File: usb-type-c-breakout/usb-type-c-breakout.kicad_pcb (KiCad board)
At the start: 4 copper layers, 29.5 x 47.5 mm, 44 parts, among them J10 USB_B_Micro, J11 USB_C_Plug, J12 Conn_02x04_Odd_Even, J2 Conn_Coaxial, J3 Conn_Coaxial, J4 Conn_Coaxial, J5 Conn_Coaxial, J6 Conn_Coaxial, J7 Conn_Coaxial, J8 Conn_Coaxial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

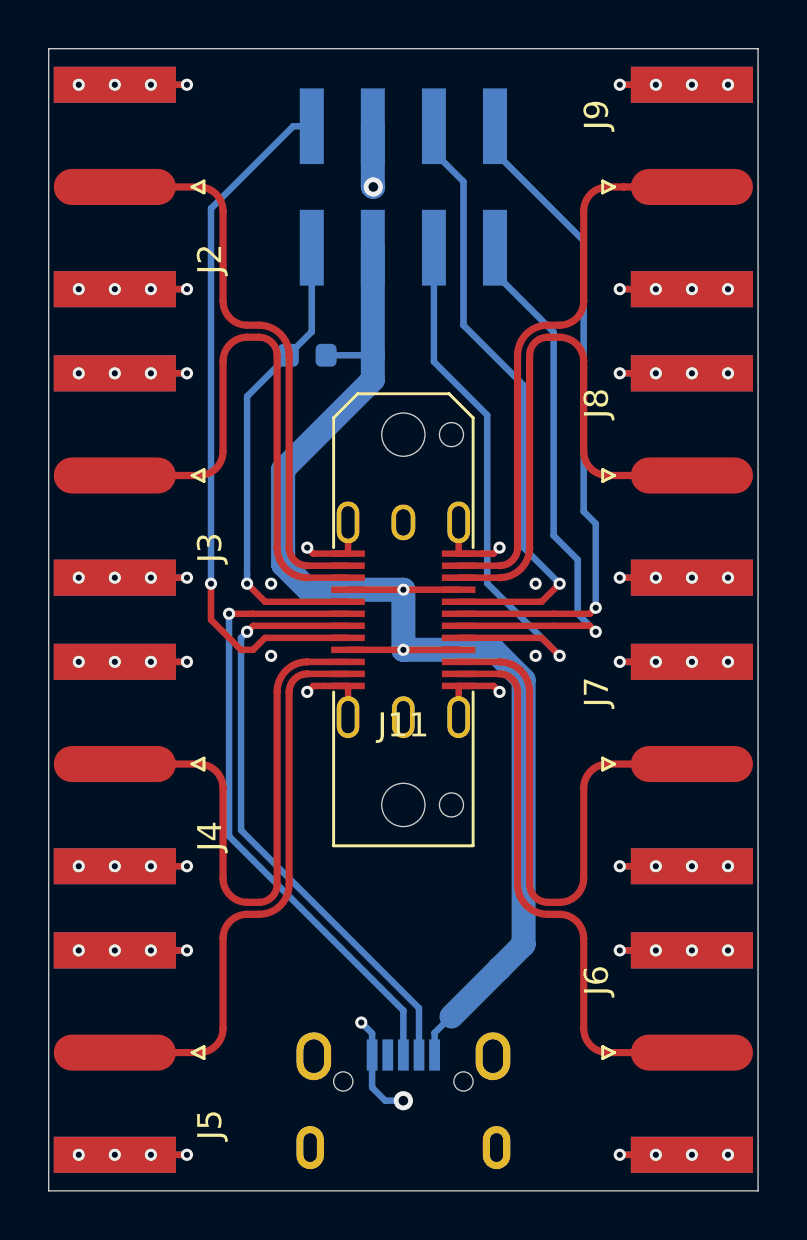
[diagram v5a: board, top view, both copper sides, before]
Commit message: assigned curve pads, added silk notes
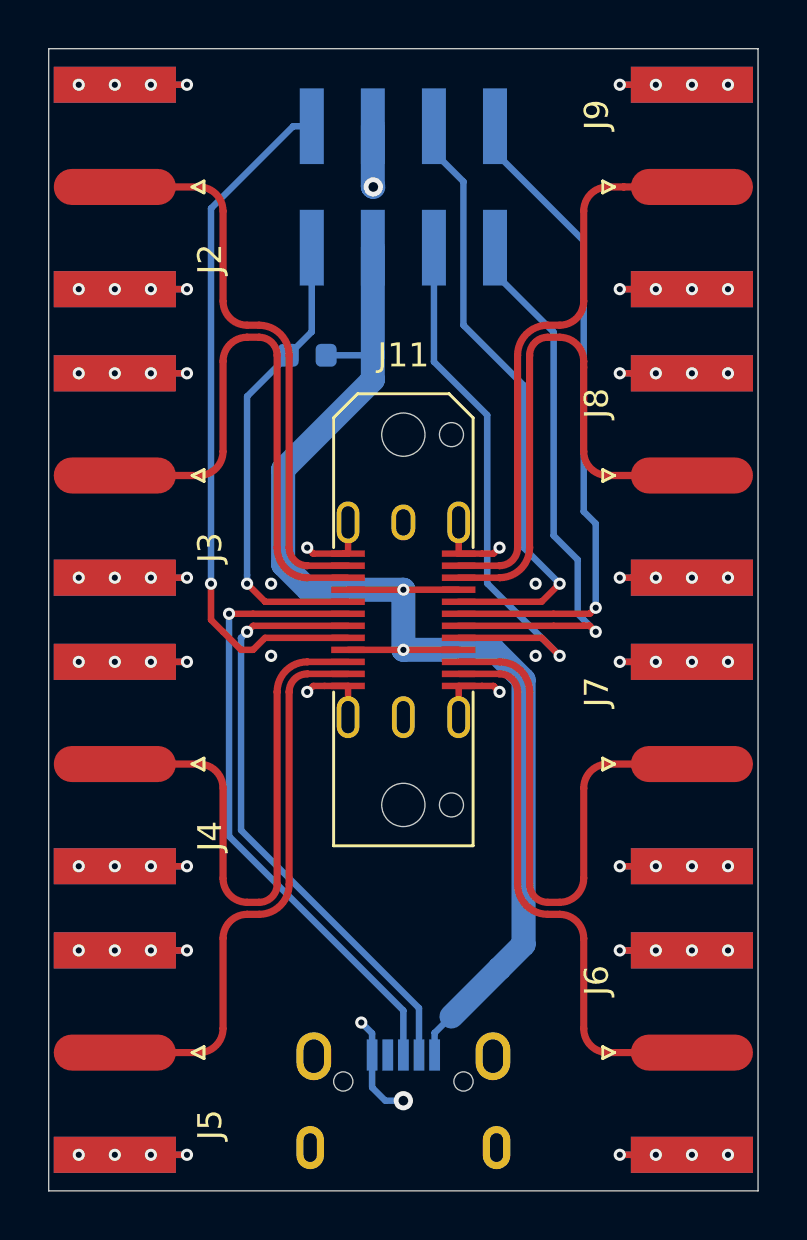
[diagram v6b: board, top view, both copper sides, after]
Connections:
- REF** pad 1: (no net) -> Net-(J11-PadB11) (x4)
- REF** pad 1: (no net) -> Net-(J11-PadA11) (x4)
- REF** pad 1: (no net) -> Net-(J11-PadA10) (x4)
- REF** pad 1: (no net) -> Net-(J11-PadA3) (x4)
- REF** pad 1: (no net) -> Net-(J11-PadA2) (x4)
- REF** pad 1: (no net) -> Net-(J11-PadB2) (x4)
- REF** pad 1: (no net) -> Net-(J11-PadB3) (x4)
- REF** pad 1: (no net) -> Net-(J11-PadB10) (x4)
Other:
- board text added: "RX1+"
- board text added: "RX1-"
- board text added: "RX2+"
- board text added: "RX2-"
- board text added: "TX1+"
- board text added: "TX1-"
- board text added: "TX2+"
- board text added: "TX2-"
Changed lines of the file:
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@@
   (general
     (thickness 1.6)
-    (drawings 4)
+    (drawings 12)
     (tracks 280)
     (modules 44)
@@
     (0 "F.Cu" signal)
     (1 "In1.Cu" signal)
-    (2 "In2.Cu" signal hide)
+    (2 "In2.Cu" signal)
     (31 "B.Cu" signal)
     (32 "B.Adhes" user)
@@
       (other_layers_text_dims (size 1 1) (thickness 0.15) keep_upright)
     )
-    (pad_size 1.5 5.08)
+    (pad_size 0.3 0.3)
     (pad_drill 0)
     (pad_to_mask_clearance 0.051)
@@
     )
     (pad "1" smd custom (at 0 1 180) (size 0.3 0.3) (layers "F.Cu")
+      (net 8 "Net-(J11-PadB11)")
       (options (clearance outline) (anchor circle))
       (primitives
@@
     )
     (pad "1" smd custom (at 0 1) (size 0.3 0.3) (layers "F.Cu")
+      (net 8 "Net-(J11-PadB11)")
       (options (clearance outline) (anchor circle))
       (primitives
@@
     )
     (pad "1" smd custom (at 0 1 90) (size 0.3 0.3) (layers "F.Cu")
+      (net 7 "Net-(J11-PadB10)")
       (options (clearance outline) (anchor circle))
       (primitives
@@
     )
     (pad "1" smd custom (at 0 1 270) (size 0.3 0.3) (layers "F.Cu")
+      (net 7 "Net-(J11-PadB10)")
       (options (clearance outline) (anchor circle))
       (primitives
@@
     )
     (pad "1" smd custom (at 0 1 180) (size 0.3 0.3) (layers "F.Cu")
+      (net 6 "Net-(J11-PadB3)")
       (options (clearance outline) (anchor circle))
       (primitives
@@
     )
     (pad "1" smd custom (at 0 1) (size 0.3 0.3) (layers "F.Cu")
+      (net 6 "Net-(J11-PadB3)")
       (options (clearance outline) (anchor circle))
       (primitives
@@
     )
     (pad "1" smd custom (at 0 1 90) (size 0.3 0.3) (layers "F.Cu")
+      (net 5 "Net-(J11-PadB2)")
       (options (clearance outline) (anchor circle))
       (primitives
@@
     )
     (pad "1" smd custom (at 0 1 270) (size 0.3 0.3) (layers "F.Cu")
+      (net 5 "Net-(J11-PadB2)")
       (options (clearance outline) (anchor circle))
       (primitives
@@
     )
     (pad "1" smd custom (at 0 1) (size 0.3 0.3) (layers "F.Cu")
+      (net 4 "Net-(J11-PadA11)")
       (options (clearance outline) (anchor circle))
       (primitives
@@
     )
     (pad "1" smd custom (at 0 1 180) (size 0.3 0.3) (layers "F.Cu")
+      (net 4 "Net-(J11-PadA11)")
       (options (clearance outline) (anchor circle))
       (primitives
@@
     )
     (pad "1" smd custom (at 0 1 270) (size 0.3 0.3) (layers "F.Cu")
+      (net 3 "Net-(J11-PadA10)")
       (options (clearance outline) (anchor circle))
       (primitives
@@
     )
     (pad "1" smd custom (at 0 1 90) (size 0.3 0.3) (layers "F.Cu")
+      (net 3 "Net-(J11-PadA10)")
       (options (clearance outline) (anchor circle))
       (primitives
@@
     )
     (pad "1" smd custom (at 0 1) (size 0.3 0.3) (layers "F.Cu")
+      (net 2 "Net-(J11-PadA3)")
       (options (clearance outline) (anchor circle))
       (primitives
@@
     )
     (pad "1" smd custom (at 0 1 180) (size 0.3 0.3) (layers "F.Cu")
+      (net 2 "Net-(J11-PadA3)")
       (options (clearance outline) (anchor circle))
       (primitives
@@
     )
     (pad "1" smd custom (at 0 1 270) (size 0.3 0.3) (layers "F.Cu")
+      (net 1 "Net-(J11-PadA2)")
       (options (clearance outline) (anchor circle))
       (primitives
@@
     )
     (pad "1" smd custom (at 0 1 90) (size 0.3 0.3) (layers "F.Cu")
+      (net 1 "Net-(J11-PadA2)")
       (options (clearance outline) (anchor circle))
       (primitives
@@
     )
     (pad "1" smd custom (at 0 1.25 90) (size 0.3 0.3) (layers "F.Cu")
+      (net 1 "Net-(J11-PadA2)")
       (options (clearance outline) (anchor circle))
       (primitives
@@
     )
     (pad "1" smd custom (at 0 1.25 270) (size 0.3 0.3) (layers "F.Cu")
+      (net 2 "Net-(J11-PadA3)")
       (options (clearance outline) (anchor circle))
       (primitives
@@
     )
     (pad "1" smd custom (at 0 1.25 180) (size 0.3 0.3) (layers "F.Cu")
+      (net 3 "Net-(J11-PadA10)")
       (options (clearance outline) (anchor circle))
       (primitives
@@
     )
     (pad "1" smd custom (at 0 1.25) (size 0.3 0.3) (layers "F.Cu")
+      (net 4 "Net-(J11-PadA11)")
       (options (clearance outline) (anchor circle))
       (primitives
@@
     )
     (pad "1" smd custom (at 0 1.25 270) (size 0.3 0.3) (layers "F.Cu")
+      (net 5 "Net-(J11-PadB2)")
       (options (clearance outline) (anchor circle))
       (primitives
@@
     )
     (pad "1" smd custom (at 0 1.25 90) (size 0.3 0.3) (layers "F.Cu")
+      (net 6 "Net-(J11-PadB3)")
       (options (clearance outline) (anchor circle))
       (primitives
@@
     )
     (pad "1" smd custom (at 0 1.25) (size 0.3 0.3) (layers "F.Cu")
+      (net 7 "Net-(J11-PadB10)")
       (options (clearance outline) (anchor circle))
       (primitives
@@
     )
     (pad "1" smd custom (at 0 1.25 180) (size 0.3 0.3) (layers "F.Cu")
+      (net 8 "Net-(J11-PadB11)")
       (options (clearance outline) (anchor circle))
       (primitives
@@
     )
     (pad "1" smd custom (at 0 0.75 180) (size 0.3 0.3) (layers "F.Cu")
+      (net 7 "Net-(J11-PadB10)")
       (options (clearance outline) (anchor circle))
       (primitives
@@
     )
     (pad "1" smd custom (at 0 0.75) (size 0.3 0.3) (layers "F.Cu")
+      (net 8 "Net-(J11-PadB11)")
       (options (clearance outline) (anchor circle))
       (primitives
@@
     )
     (pad "1" smd custom (at 0 0.75 270) (size 0.3 0.3) (layers "F.Cu")
+      (net 6 "Net-(J11-PadB3)")
       (options (clearance outline) (anchor circle))
       (primitives
@@
     )
     (pad "1" smd custom (at 0 0.75 90) (size 0.3 0.3) (layers "F.Cu")
+      (net 5 "Net-(J11-PadB2)")
       (options (clearance outline) (anchor circle))
       (primitives
@@
     )
     (pad "1" smd custom (at 0 0.75 180) (size 0.3 0.3) (layers "F.Cu")
+      (net 4 "Net-(J11-PadA11)")
       (options (clearance outline) (anchor circle))
       (primitives
@@
     )
     (pad "1" smd custom (at 0 0.75) (size 0.3 0.3) (layers "F.Cu")
+      (net 3 "Net-(J11-PadA10)")
       (options (clearance outline) (anchor circle))
       (primitives
@@
     )
     (pad "1" smd custom (at 0 0.75 90) (size 0.3 0.3) (layers "F.Cu")
+      (net 2 "Net-(J11-PadA3)")
       (options (clearance outline) (anchor circle))
       (primitives
@@
     )
     (pad "1" smd custom (at 0 0.75 270) (size 0.3 0.3) (layers "F.Cu")
+      (net 1 "Net-(J11-PadA2)")
       (options (clearance outline) (anchor circle))
       (primitives
@@
     (at 100 100 90)
     (attr smd)
-    (fp_text reference "J11" (at -4.385 0 180) (layer "F.SilkS")
+    (fp_text reference "J11" (at 11 0 180) (layer "F.SilkS")
       (effects (font (size 1 1) (thickness 0.15)))
     )
@@
     )
   )
+  (gr_text "RX1+" (at 112 82) (layer "B.SilkS")
+    (effects (font (size 1 1) (thickness 0.15)) (justify mirror))
+  )
+  (gr_text "RX1-" (at 112 94) (layer "B.SilkS")
+    (effects (font (size 1 1) (thickness 0.15)) (justify mirror))
+  )
+  (gr_text "TX2-" (at 112 106) (layer "B.SilkS")
+    (effects (font (size 1 1) (thickness 0.15)) (justify mirror))
+  )
+  (gr_text "TX2+" (at 112 118) (layer "B.SilkS")
+    (effects (font (size 1 1) (thickness 0.15)) (justify mirror))
+  )
+  (gr_text "RX2+" (at 88 118) (layer "B.SilkS")
+    (effects (font (size 1 1) (thickness 0.15)) (justify mirror))
+  )
+  (gr_text "RX2-" (at 88 106) (layer "B.SilkS")
+    (effects (font (size 1 1) (thickness 0.15)) (justify mirror))
+  )
+  (gr_text "TX1-" (at 88 94) (layer "B.SilkS")
+    (effects (font (size 1 1) (thickness 0.15)) (justify mirror))
+  )
+  (gr_text "TX1+" (at 88 82) (layer "B.SilkS")
+    (effects (font (size 1 1) (thickness 0.15)) (justify mirror))
+  )
   (gr_line (start 85.25 123.75) (end 85.25 76.25) (layer "Edge.Cuts") (width 0.05))
